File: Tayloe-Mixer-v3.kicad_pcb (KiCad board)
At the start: 2 copper layers, 112 x 78.5 mm, 61 parts, among them J1 BNC, J101 Audio_Jack, J2 Conn_01x04, J3 Pad, J4 Conn_01x07_Female, J5 Pad, Q1 2N3904-SMD, Q2 2N3904-SMD, SW1 SW_DIP_x01, SW2 Rotary_Encoder_Switch, T1 6:31, T2 31:6, T3 T50_SPLITTER, U1 ESP32-A1S, U2 FST3253, U201 MAR6, U3 LM4562, U4 si5351, U5 L7805, U7 AMS1117CD-3.3

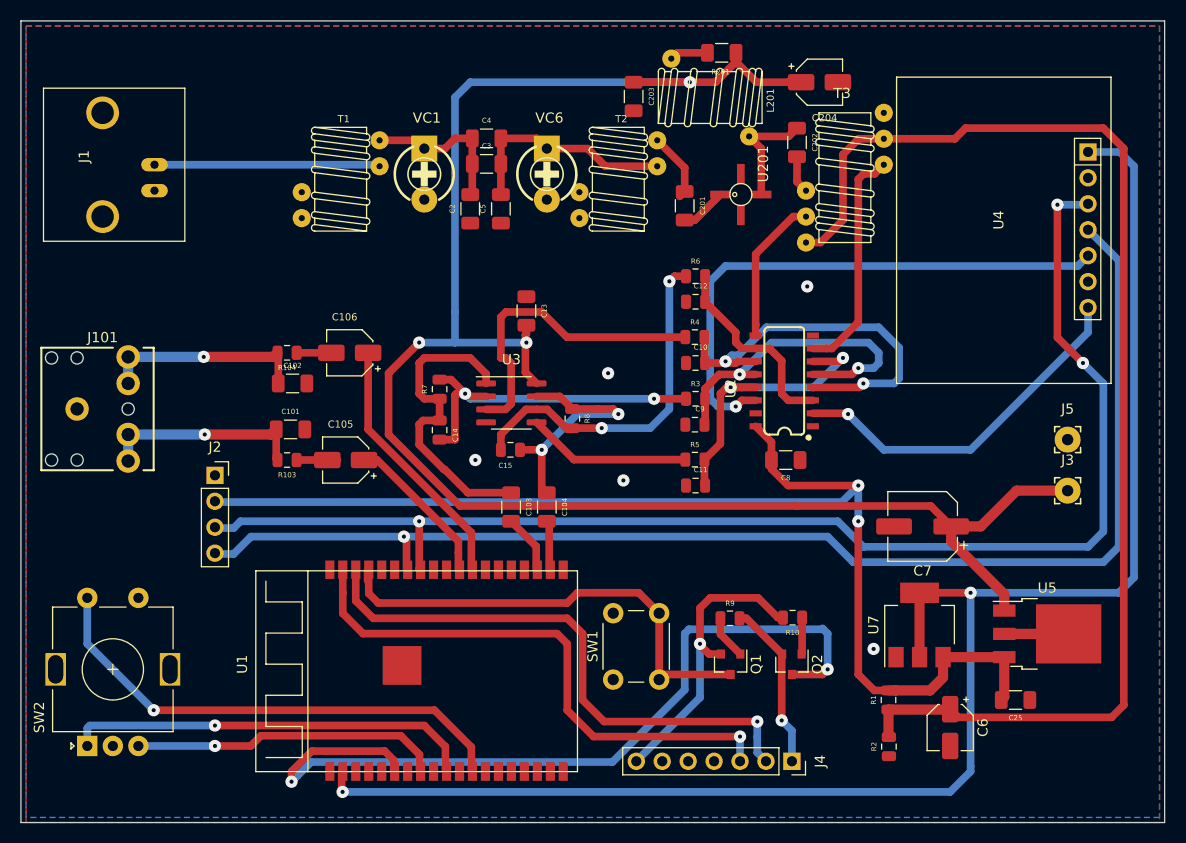
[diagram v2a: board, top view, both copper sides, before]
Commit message: moved bpf
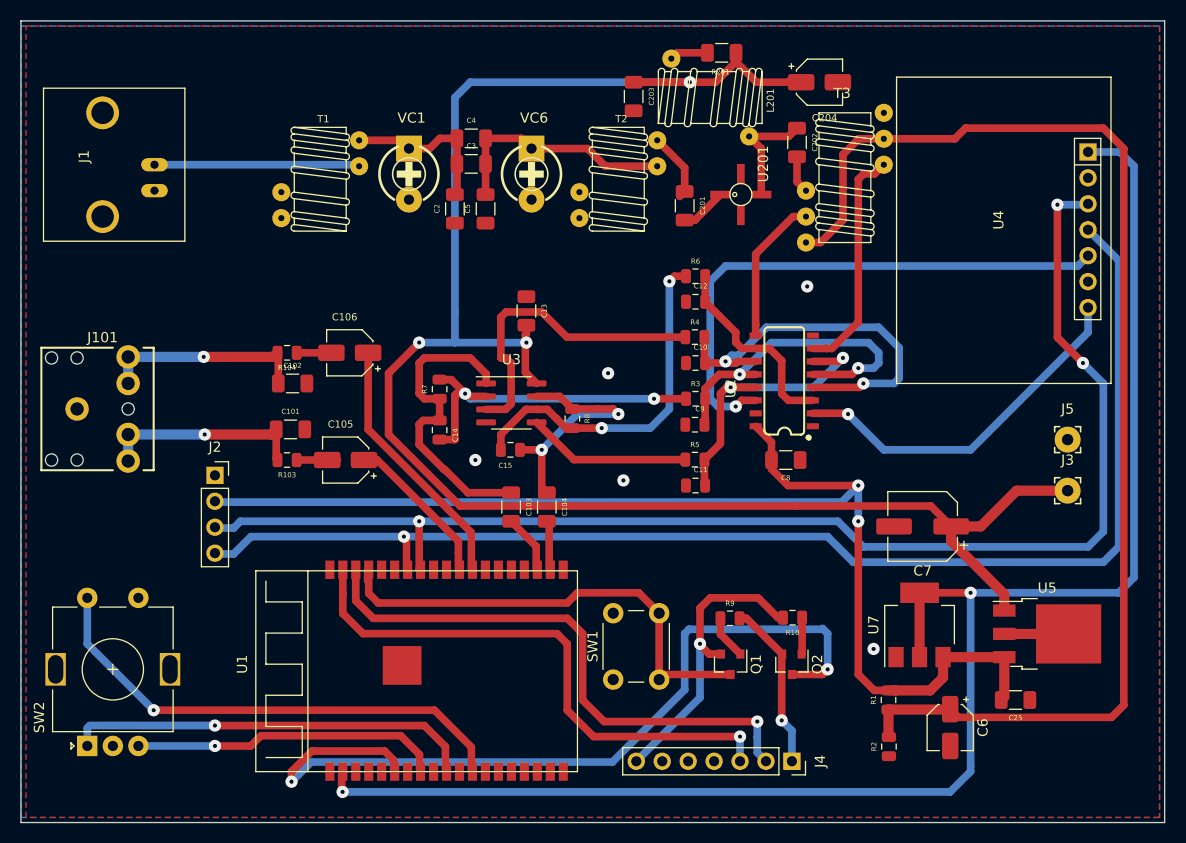
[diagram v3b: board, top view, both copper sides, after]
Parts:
- moved T1 2.00 mm to (73.8, 33.5)
- moved C2 1.50 mm to (84.8, 43.4)
- moved C3 1.50 mm to (88.6, 36.8)
- moved C4 1.50 mm to (88.6, 34.2)
- moved C5 1.50 mm to (87.8, 43.4)
- moved VC1 1.50 mm to (82.5, 33.5)
- moved VC6 1.50 mm to (94.5, 33.5)
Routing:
- net Net-(J1-PadS): track 22.1 -> 20.3 mm
- net Net-(C3-Pad2): track 21.9 -> 23.4 mm
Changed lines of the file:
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@@
     (thickness 1.6)
     (drawings 4)
-    (tracks 456)
+    (tracks 457)
     (zones 0)
     (modules 61)
@@
   )
   (module Xenir:trimcap (layer F.Cu)
-    (at 96 33.5)
+    (at 94.5 33.5)
     (fp_text reference VC6 (at 0.25 1) (layer F.SilkS)
       (effects (font (size 1 1) (thickness 0.15)))
@@
   )
   (module Xenir:trimcap (layer F.Cu)
-    (at 84 33.5)
+    (at 82.5 33.5)
     (fp_text reference VC1 (at 0.25 1) (layer F.SilkS)
       (effects (font (size 1 1) (thickness 0.15)))
@@
   )
   (module "Xenir:T37 Transformer" (layer F.Cu)
-    (at 75.81 33.5)
+    (at 73.81 33.5)
     (fp_text reference T1 (at 0.3 1.1) (layer F.SilkS)
       (effects (font (size 0.7 0.7) (thickness 0.15)))
@@
   )
   (module "Xenir:Capacitor 1206" (layer F.Cu)
-    (at 89.25 43.4 90)
+    (at 87.75 43.4 90)
     (fp_text reference C5 (at 0 0.5 90) (layer F.SilkS)
       (effects (font (size 0.5 0.5) (thickness 0.125)))
@@
   )
   (module "Xenir:Capacitor 1206" (layer F.Cu)
-    (at 90.1 34.25)
+    (at 88.6 34.25)
     (fp_text reference C4 (at 0 0.5) (layer F.SilkS)
       (effects (font (size 0.5 0.5) (thickness 0.125)))
@@
   )
   (module "Xenir:Capacitor 1206" (layer F.Cu)
-    (at 90.1 36.75)
+    (at 88.6 36.75)
     (fp_text reference C3 (at 0 0.5) (layer F.SilkS)
       (effects (font (size 0.5 0.5) (thickness 0.125)))
@@
   )
   (module "Xenir:Capacitor 1206" (layer F.Cu)
-    (at 86.25 43.4 90)
+    (at 84.75 43.4 90)
     (fp_text reference C2 (at 0 0.5 90) (layer F.SilkS)
       (effects (font (size 0.5 0.5) (thickness 0.125)))
@@
   (via (at 110 31) (size 1.2) (drill 0.4) (layers F.Cu B.Cu) (net 3))
   (segment (start 110 31) (end 88.5 31) (width 0.75) (layer B.Cu) (net 3))
-  (segment (start 88.5 31) (end 87 32.5) (width 0.75) (layer B.Cu) (net 3))
   (segment (start 87 32.5) (end 87 53.5) (width 0.75) (layer B.Cu) (net 3))
   (segment (start 87 53.5) (end 87 56.5) (width 0.75) (layer B.Cu) (net 3))
@@
   (segment (start 142 71) (end 138.5 74.5) (width 1) (layer F.Cu) (net 3))
   (segment (start 147 71) (end 142 71) (width 1) (layer F.Cu) (net 3))
+  (segment (start 88.5 31) (end 87 32.5) (width 0.75) (layer B.Cu) (net 3))
   (segment (start 132.5 81) (end 132.5 87.3) (width 1) (layer F.Cu) (net 4))
   (segment (start 137.5 81) (end 137.5 81) (width 0.75) (layer B.Cu) (net 4))
@@
   (segment (start 110.5 44.5) (end 113 42) (width 0.75) (layer F.Cu) (net 49))
   (segment (start 109.5 44.5) (end 110.5 44.5) (width 0.75) (layer F.Cu) (net 49))
-  (segment (start 83.19 36.69) (end 84 37.5) (width 0.75) (layer F.Cu) (net 50))
-  (segment (start 79.62 36.69) (end 83.19 36.69) (width 0.75) (layer F.Cu) (net 50))
-  (segment (start 86.02 37.5) (end 87.02 36.5) (width 0.75) (layer F.Cu) (net 50))
-  (segment (start 87.02 36.5) (end 88.7 36.5) (width 0.75) (layer F.Cu) (net 50))
-  (segment (start 84 37.5) (end 86.02 37.5) (width 0.75) (layer F.Cu) (net 50))
-  (segment (start 88.7 36.5) (end 88.7 39) (width 0.75) (layer F.Cu) (net 50))
-  (segment (start 88.7 41.8) (end 88.5 42) (width 0.75) (layer F.Cu) (net 50))
-  (segment (start 88.7 39) (end 88.7 41.8) (width 0.75) (layer F.Cu) (net 50))
-  (segment (start 91.5 42) (end 91.5 39) (width 0.75) (layer F.Cu) (net 51))
-  (segment (start 95 36.5) (end 96 37.5) (width 0.75) (layer F.Cu) (net 51))
-  (segment (start 91.5 36.5) (end 95 36.5) (width 0.75) (layer F.Cu) (net 51))
-  (segment (start 96 37.5) (end 100 37.5) (width 0.75) (layer F.Cu) (net 51))
+  (segment (start 84.52 37.5) (end 85.52 36.5) (width 0.75) (layer F.Cu) (net 50))
+  (segment (start 85.52 36.5) (end 87.2 36.5) (width 0.75) (layer F.Cu) (net 50))
+  (segment (start 82.5 37.5) (end 84.52 37.5) (width 0.75) (layer F.Cu) (net 50))
+  (segment (start 87.2 36.5) (end 87.2 39) (width 0.75) (layer F.Cu) (net 50))
+  (segment (start 87.2 41.8) (end 87 42) (width 0.75) (layer F.Cu) (net 50))
+  (segment (start 87.2 39) (end 87.2 41.8) (width 0.75) (layer F.Cu) (net 50))
+  (segment (start 81.69 36.69) (end 82.5 37.5) (width 0.75) (layer F.Cu) (net 50))
+  (segment (start 77.62 36.69) (end 81.69 36.69) (width 0.75) (layer F.Cu) (net 50))
+  (segment (start 90 42) (end 90 39) (width 0.75) (layer F.Cu) (net 51))
+  (segment (start 93.5 36.5) (end 94.5 37.5) (width 0.75) (layer F.Cu) (net 51))
+  (segment (start 90 36.5) (end 93.5 36.5) (width 0.75) (layer F.Cu) (net 51))
   (segment (start 101.73 39.23) (end 106.81 39.23) (width 0.75) (layer F.Cu) (net 51))
   (segment (start 100 37.5) (end 101.73 39.23) (width 0.75) (layer F.Cu) (net 51))
-  (segment (start 91.5 36.5) (end 91.5 39) (width 0.75) (layer F.Cu) (net 51))
+  (segment (start 90 36.5) (end 90 39) (width 0.75) (layer F.Cu) (net 51))
+  (segment (start 94.5 37.5) (end 100 37.5) (width 0.75) (layer F.Cu) (net 51))
   (segment (start 111.5 64.4775) (end 111.4375 64.54) (width 0.75) (layer F.Cu) (net 52))
   (segment (start 111.5 62) (end 111.5 64.4775) (width 0.75) (layer F.Cu) (net 52))
@@
   (segment (start 120.5 40.74) (end 121.38 41.62) (width 0.75) (layer F.Cu) (net 59))
   (segment (start 120.5 38.3) (end 120.5 40.74) (width 0.75) (layer F.Cu) (net 59))
-  (segment (start 79.47 39.08) (end 79.62 39.23) (width 0.75) (layer B.Cu) (net 60))
-  (segment (start 57.58 39.08) (end 79.47 39.08) (width 0.75) (layer B.Cu) (net 60))
+  (segment (start 57.73 39.23) (end 57.58 39.08) (width 0.75) (layer B.Cu) (net 60))
+  (segment (start 77.47 39.08) (end 77.62 39.23) (width 0.75) (layer B.Cu) (net 60))
+  (segment (start 57.58 39.08) (end 77.47 39.08) (width 0.75) (layer B.Cu) (net 60))
   (segment (start 106.54 55.96) (end 106.54 55.96) (width 0.75) (layer F.Cu) (net 61))
   (segment (start 92.5 58.5) (end 92.5 58.5) (width 0.75) (layer F.Cu) (net 61))
@@
     )
   )
-  (zone (net 1) (net_name GND) (layer F.Cu) (hatch edge 0.508)
+  (zone (net 1) (net_name GND) (layer B.Cu) (hatch edge 0.508)
     (connect_pads (clearance 0.508))
     (min_thickness 0.254)
@@
     (polygon
       (pts
-        (xy 156 103.5) (xy 45 103.5) (xy 45 25.5) (xy 156 25.5)
+        (xy 156 103) (xy 44.5 103) (xy 44.5 25.5) (xy 156 25.5)
       )
     )
   )
-  (zone (net 1) (net_name GND) (layer B.Cu) (hatch edge 0.508)
+  (zone (net 1) (net_name GND) (layer F.Cu) (hatch edge 0.508)
     (connect_pads (clearance 0.508))
     (min_thickness 0.254)
